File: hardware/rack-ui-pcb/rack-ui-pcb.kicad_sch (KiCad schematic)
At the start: 8 parts, among them J1 IO, J2 Conn_ARM_SWD_TagConnect_TC203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, SW1 RotaryEncoder_Switch_MP, U1 PY32F002AL15S6TU

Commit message: updated schematic & PCB
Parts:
- added H1, H2, H3, H4: MountingHole_M3_3.2mm_Pad, PCM_SL_Mechanical:MountingHole_3.2mm_Pad, symbol PCM_SL_Mechanical:MountingHole_M3_3.2mm_Pad
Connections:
- net +3.3V is gone; now on net +3V3: C3.1, J2.1 (VCC), U1.1 (VCC)
- net SDA is gone; now on net RST: J1.8 (Pin_8), OLED1.4 (SDA)
- net SWD is gone; now on net EncSW: J2.2 (SWDIO), U1.5 (PA13-SWD)
- net EncA: now also U1.2 (PA4/PA10)
- net EncB: now also U1.7 (PA1)
- net GND: now also SW1.MP, H1.1, H2.1, H3.1, H4.1
- net SCL: now also U1.3 (PA3)

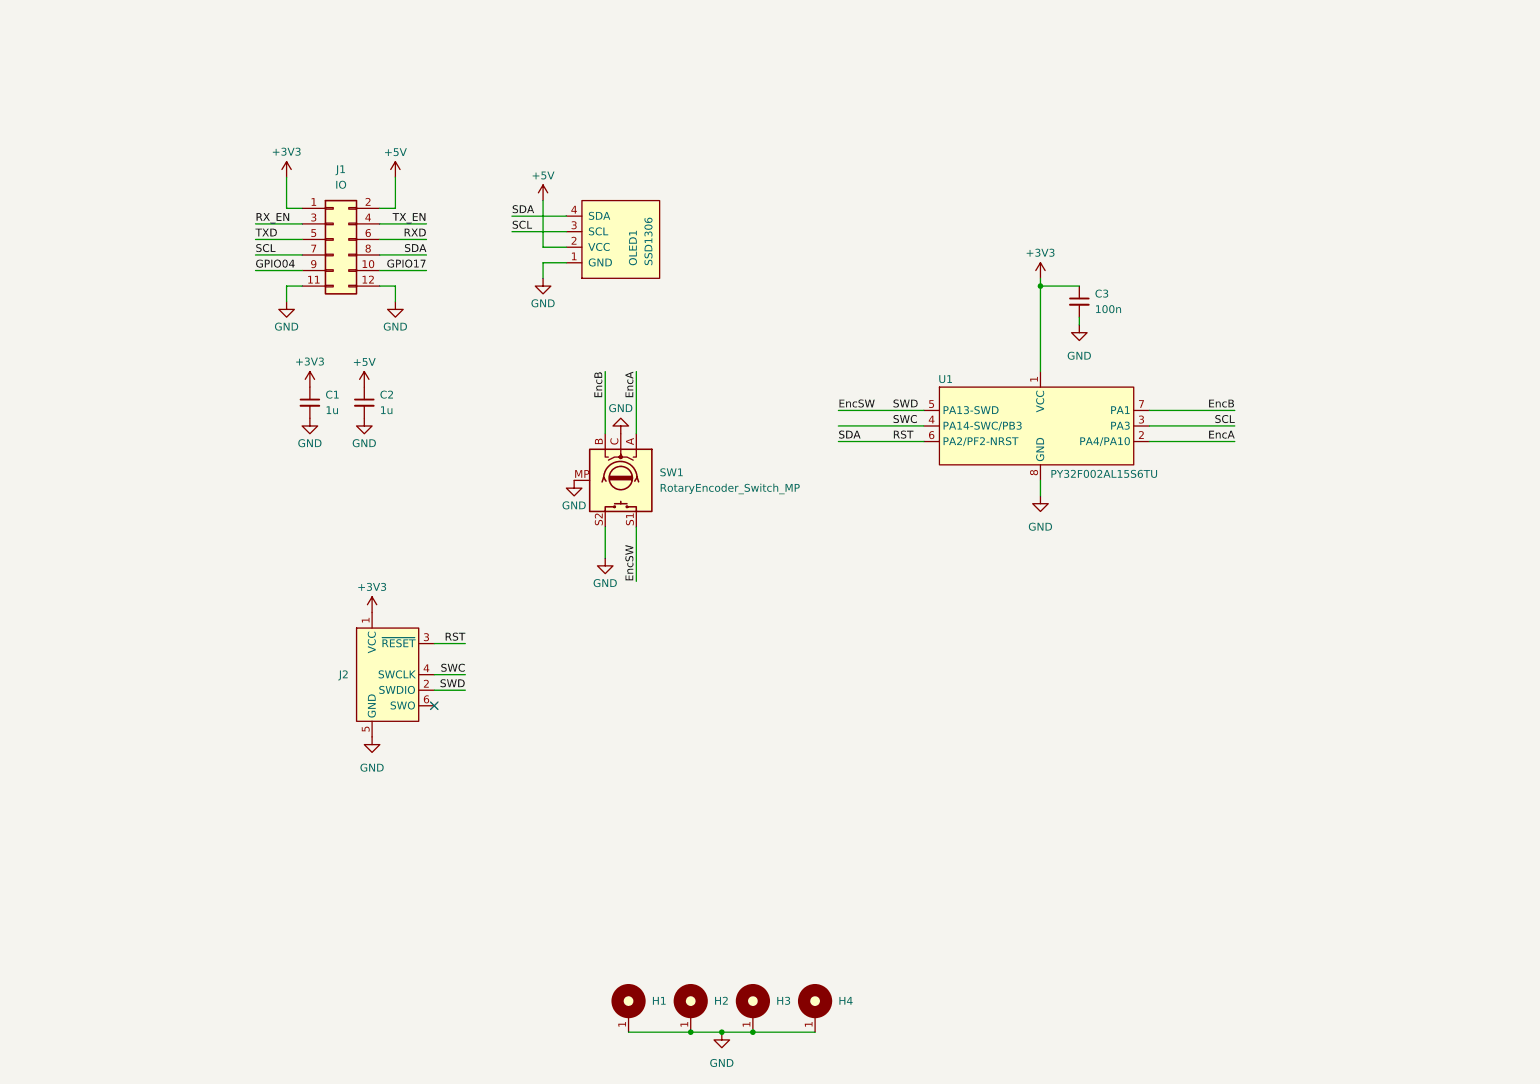
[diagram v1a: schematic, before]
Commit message: updated design wih new uC, added USB-C and UART chip
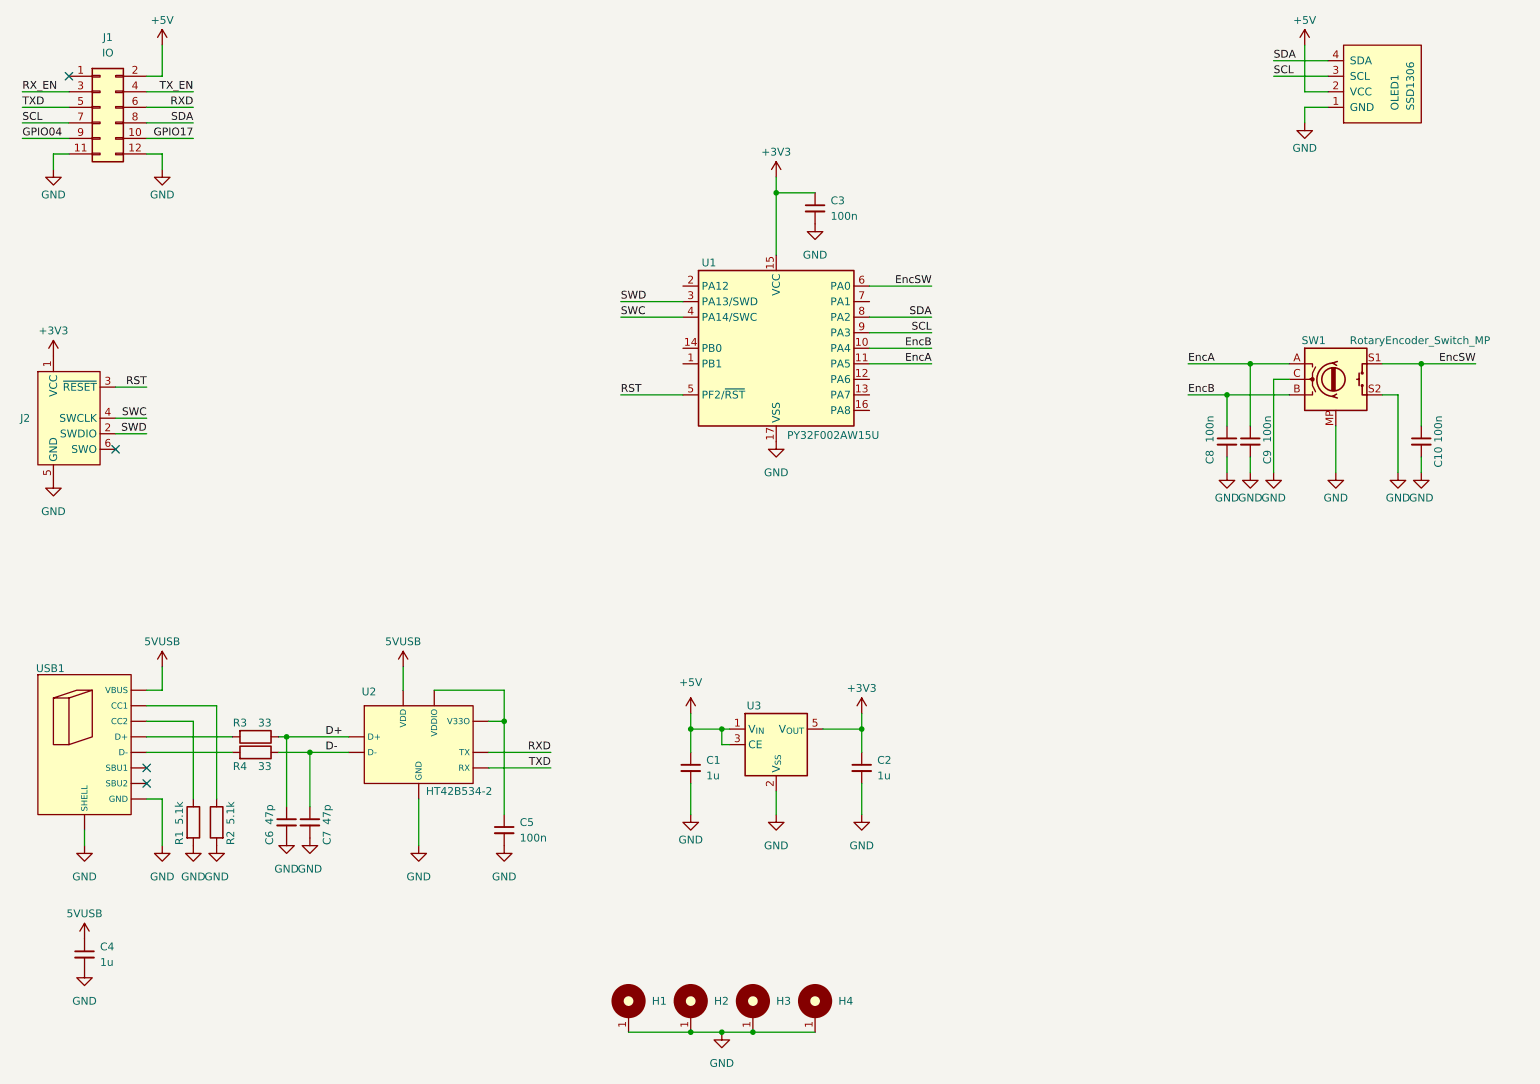
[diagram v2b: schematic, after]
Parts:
- removed U1: PY32F002AL15S6TU, PY32:SOP-8_L4.9-W3.9-P1.27-LS6.0-BL-1, symbol PY32:PY32F002AL15S6TU
- added C10, C5, C8, C9: 100n, Capacitor_SMD:C_0603_1608Metric_Pad1.08x0.95mm_HandSolder, symbol Device:C_Small
- added C4: 1u, Capacitor_SMD:C_0603_1608Metric_Pad1.08x0.95mm_HandSolder, symbol Device:C_Small
- added C6, C7: 47p, Capacitor_SMD:C_0603_1608Metric_Pad1.08x0.95mm_HandSolder, symbol Device:C_Small
- added R1, R2: 5.1k, Resistor_SMD:R_0603_1608Metric_Pad0.98x0.95mm_HandSolder, symbol Device:R
- added R3, R4: 33, Resistor_SMD:R_0603_1608Metric_Pad0.98x0.95mm_HandSolder, symbol Device:R
- added U1: PY32F002AW15U, Package_DFN_QFN:WQFN-16-1EP_3x3mm_P0.5mm_EP1.75x1.75mm, symbol MCU_Puya:PY32F002AW15U
- added U2: HT42B534-2, LCSC:SOP-8_L4.9-W3.9-P1.27-LS6.0-BL, symbol LCSC:HT42B534-2
- added U3: ME6211C33M5G-N, LCSC:SOT-23-5_L3.0-W1.7-P0.95-LS2.8-BL, symbol LCSC:ME6211C33M5G-N
- added USB1: JS16H-TYPE-C449-H105, LCSC:USB-TH_JS16H-TYPE-C449-H105-1, symbol LCSC:JS16H-TYPE-C449-H105
- C1, C2, C3: footprint Capacitor_SMD:C_0402_1005Metric_Pad0.74x0.62mm_HandSolder -> Capacitor_SMD:C_0603_1608Metric_Pad1.08x0.95mm_HandSolder
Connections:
- net +3V3: now also C2.1, U1.15 (VCC), U3.5 (V_{OUT}); no longer C1.1, J1.1 (Pin_1)
- net +5V: now also C1.1, U3.1 (V_{IN}), U3.3 (CE); no longer C2.1
- net EncA: now also C9.1, U1.11 (PA5)
- net EncB: now also C8.1, U1.10 (PA4)
- net EncSW: now also C10.1, U1.6 (PA0); no longer J2.2 (SWDIO)
- net GND: now also C10.2, C4.2, C5.2, C6.2, C7.2, C8.2, C9.2, R1.2, R2.2, U1.17 (VSS), U2.1 (GND), U3.2 (V_{SS}), USB1.1 (SHELL), USB1.2 (SHELL), USB1.3 (SHELL), USB1.4 (SHELL), USB1.A1 (GND), USB1.A12 (GND), USB1.B1 (GND), USB1.B12 (GND)
- net RST: now also U1.5 (PF2/~{RST}); no longer J1.8 (Pin_8), OLED1.4 (SDA)
- net RXD: now also U2.2 (TX)
- net SCL: now also U1.9 (PA3)
- net SWC: now also U1.4 (PA14/SWC)
- net TXD: now also U2.4 (RX)
- new net: R2.1, USB1.A5 (CC1)
- new net: R3.2, USB1.A6 (D+), USB1.B6 (D+)
- new net: R4.2, USB1.A7 (D-), USB1.B7 (D-)
- new net: R1.1, USB1.B5 (CC2)
- new net: C5.1, U2.3 (VDDIO), U2.8 (V33O)
- new net 5VUSB: C4.1, U2.7 (VDD), USB1.A4 (VBUS), USB1.A9 (VBUS), USB1.B4 (VBUS), USB1.B9 (VBUS)
- new net D+: C6.1, R3.1, U2.5 (D+)
- new net D-: C7.1, R4.1, U2.6 (D-)
- new net SDA: J1.8 (Pin_8), OLED1.4 (SDA), U1.8 (PA2)
- new net SWD: J2.2 (SWDIO), U1.3 (PA13/SWD)
- no-connect marks 1 -> 4
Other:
- moved on the sheet: C3, J1, J2, OLED1

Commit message: added charlieplexed LED matrix
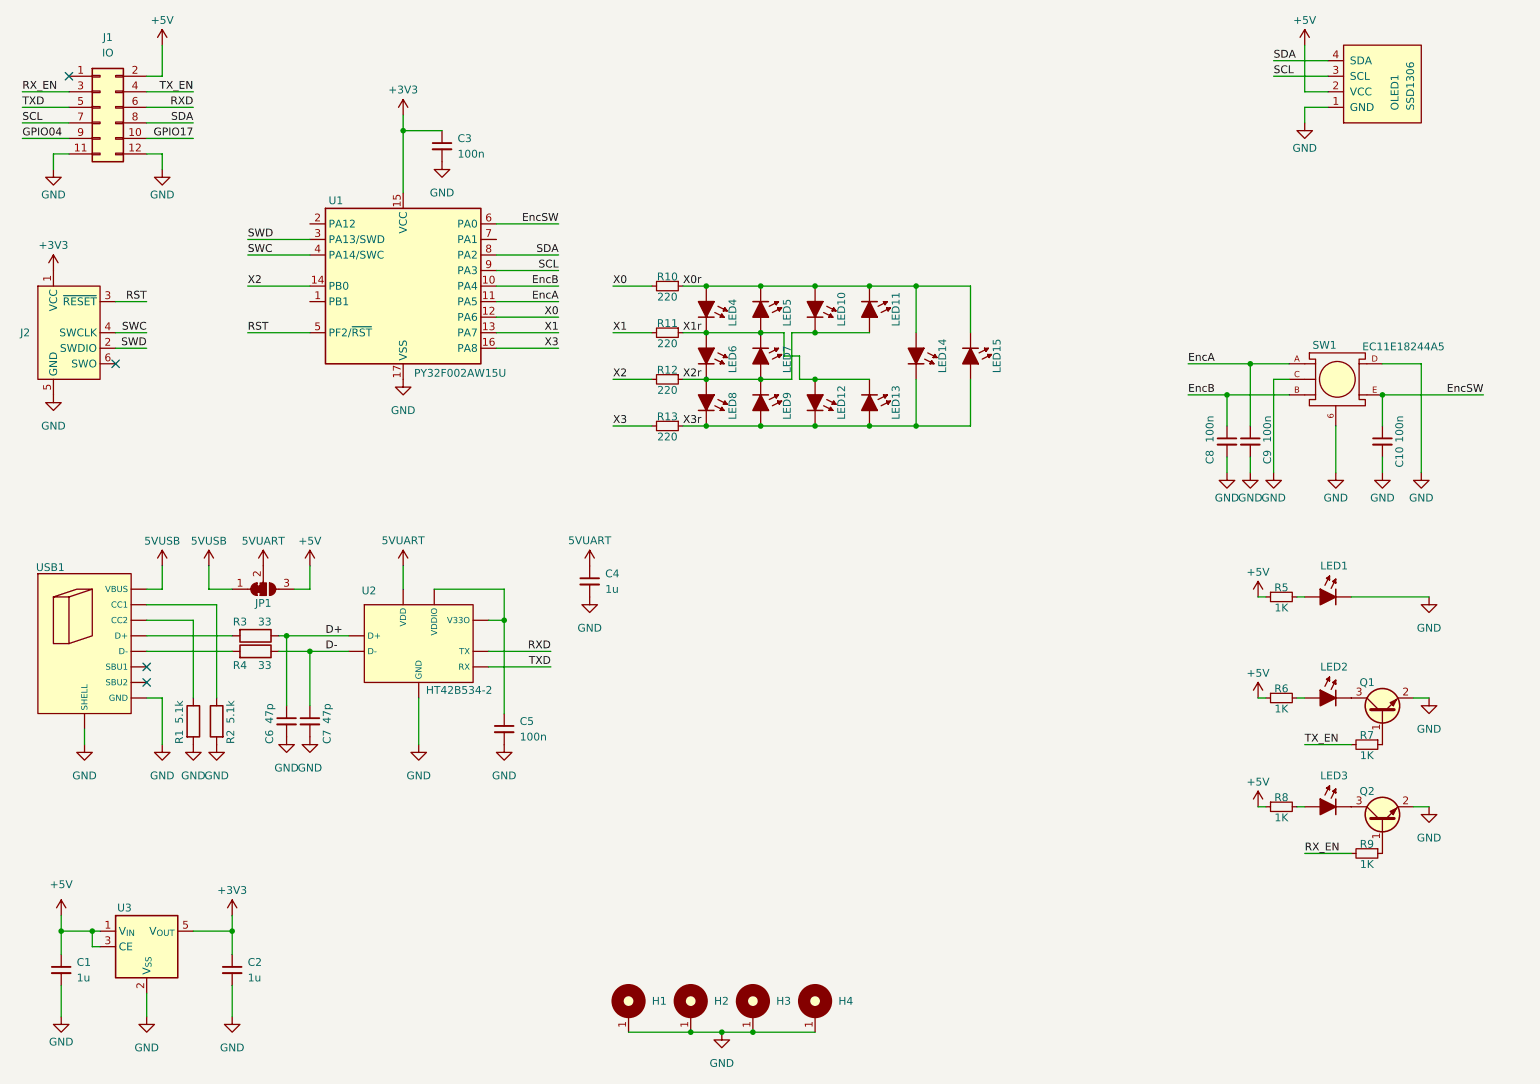
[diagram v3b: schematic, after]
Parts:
- removed SW1: RotaryEncoder_Switch_MP, Rotary_Encoder:RotaryEncoder_Alps_EC11E-Switch_Vertical_H20mm, symbol Device:RotaryEncoder_Switch_MP
- added JP1: SolderJumper_3_Bridged12, Jumper:SolderJumper-3_P1.3mm_Bridged12_RoundedPad1.0x1.5mm, symbol Jumper:SolderJumper_3_Bridged12
- added LED1, LED10, LED11, LED12, LED13, LED14, LED15, LED4, LED5, LED6, LED7, LED8, LED9: Red, PCM_LED_SMD_AKL:LED_0402_1005Metric_Pad0.77x0.64mm, symbol PCM_LED_AKL:LED_0603
- added LED2: Amber, PCM_LED_SMD_AKL:LED_0402_1005Metric_Pad0.77x0.64mm, symbol PCM_LED_AKL:LED_0603
- added LED3: Green, PCM_LED_SMD_AKL:LED_0402_1005Metric_Pad0.77x0.64mm, symbol PCM_LED_AKL:LED_0603
- added Q1, Q2: BC817-40W, Package_TO_SOT_SMD:SOT-323_SC-70, symbol PCM_Transistor_BJT_AKL:BC817-40W
- added R10, R11, R12, R13: 220, Resistor_SMD:R_0603_1608Metric_Pad0.98x0.95mm_HandSolder, symbol Device:R_Small
- added R5, R6, R7, R8, R9: 1K, Resistor_SMD:R_0603_1608Metric_Pad0.98x0.95mm_HandSolder, symbol Device:R_Small
- added SW1: EC11E18244A5, LCSC:SW-TH_EC11E18244A5, symbol LCSC:EC11E18244A5
- J1: footprint Connector_IDC:IDC-Header_2x06_P2.54mm_Horizontal -> Connector_IDC:IDC-Header_2x06_P2.54mm_Vertical
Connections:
- net +5V: now also JP1.3 (B), R5.1, R6.1, R8.1
- net 5VUSB: now also JP1.1 (A); no longer C4.1, U2.7 (VDD)
- net EncA: now also SW1.A
- net EncB: now also SW1.B
- net EncSW: now also SW1.E
- net GND: now also LED1.1 (K), Q1.2 (E), Q2.2 (E), SW1.6, SW1.7, SW1.C, SW1.D
- net RX_EN: now also R9.2
- net TX_EN: now also R7.2
- net X0: now reaches U1.12 (PA6)
- net X0: now also R10.2
- net X1: now reaches U1.13 (PA7)
- net X1: now also R11.2
- net X2: now reaches U1.14 (PB0)
- net X2: now also R12.2
- net X3: now reaches U1.16 (PA8)
- net X3: now also R13.2
- new net: Q1.1 (B), R7.1
- new net: Q2.1 (B), R9.1
- new net: LED3.1 (K), Q2.3 (C)
- new net: LED2.1 (K), Q1.3 (C)
- new net: LED2.2 (A), R6.2
- new net: LED1.2 (A), R5.2
- new net: LED3.2 (A), R8.2
- new net 5VUART: C4.1, JP1.2 (C), U2.7 (VDD)
- new net X0r: LED10.2 (A), LED11.1 (K), LED14.2 (A), LED15.1 (K), LED4.2 (A), LED5.1 (K), R10.1
- new net X1r: LED12.2 (A), LED13.1 (K), LED4.1 (K), LED5.2 (A), LED6.2 (A), LED7.1 (K), R11.1
- new net X2r: LED10.1 (K), LED11.2 (A), LED6.1 (K), LED7.2 (A), LED8.2 (A), LED9.1 (K), R12.1
- new net X3r: LED12.1 (K), LED13.2 (A), LED14.1 (K), LED15.2 (A), LED8.1 (K), LED9.2 (A), R13.1
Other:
- moved on the sheet: C1, C10, C2, C3, C4, C5, C6, C7, J2, R1, R2, R3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

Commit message: updated white LED footprints
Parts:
- LED10, LED11, LED12, LED13, LED14, LED15, LED5, LED6, LED7, LED8, LED9: footprint PCM_LED_SMD_AKL:LED_0402_1005Metric_Pad0.77x0.64mm -> LED_SMD:LED_0805_2012Metric_Pad1.15x1.40mm_HandSolder
- LED4: value Red -> SZYY0805W; footprint PCM_LED_SMD_AKL:LED_0402_1005Metric_Pad0.77x0.64mm -> LED_SMD:LED_0805_2012Metric_Pad1.15x1.40mm_HandSolder; LCSC Part C7496803 -> C434434
- R10, R11, R12, R13: value 220 -> 120
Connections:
- net X2: now also U1.2 (PA12); no longer U1.14 (PB0)
- no-connect marks 4 -> 7
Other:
- moved on the sheet: C3, C4, LED10, LED11, LED12, LED13, LED14, LED15, LED4, LED5, LED6, LED7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

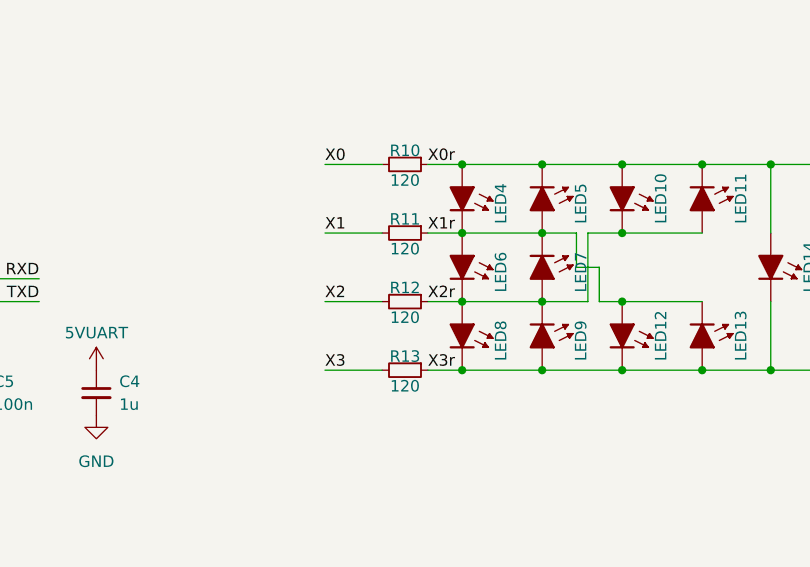
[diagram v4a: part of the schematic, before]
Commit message: updated footprints, part numbers
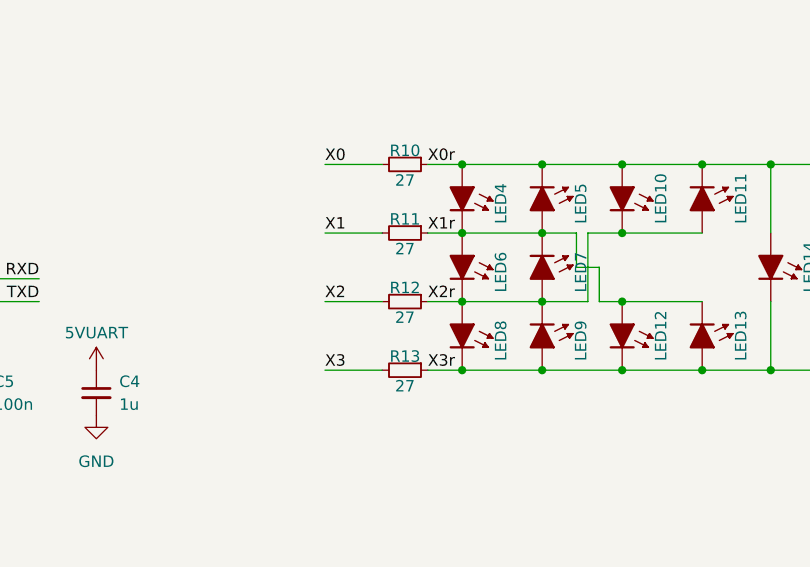
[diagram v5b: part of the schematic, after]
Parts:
- C1, C2, C4: LCSC (none) -> C59302; LCSC Part C29266 -> C59302
- C10, C3, C5, C8, C9: LCSC (none) -> C235731; LCSC Part C60474 -> C235731
- C6, C7: LCSC (none) -> C1671; LCSC Part C60474 -> C1671
- J1: LCSC (none) -> C109410; LCSC Part (none) -> C109410; now in the parts list
- LED1: footprint PCM_LED_SMD_AKL:LED_0402_1005Metric_Pad0.77x0.64mm -> PCM_SparkFun-LED:LED_0603_1608Metric_Red; LCSC (none) -> C52675987; LCSC Part C7496803 -> C52675987
- LED10, LED11, LED12, LED13, LED14, LED15, LED5, LED6, LED7, LED8, LED9: value Red -> SZYY0805W; LCSC (none) -> C434434; LCSC Part C7496803 -> C434434
- LED2: footprint PCM_LED_SMD_AKL:LED_0402_1005Metric_Pad0.77x0.64mm -> PCM_SparkFun-LED:LED_0603_1608Metric_Orange; LCSC (none) -> C165983; LCSC Part C5123495 -> C165983
- LED3: footprint PCM_LED_SMD_AKL:LED_0402_1005Metric_Pad0.77x0.64mm -> PCM_SparkFun-LED:LED_0603_1608Metric_Green; LCSC (none) -> C51933293; LCSC Part C74338 -> C51933293
- LED4: LCSC (none) -> C434434
- OLED1: now left out of the parts list
- Q1, Q2: LCSC (none) -> C383187
- R1, R2: LCSC (none) -> C2907114; LCSC Part (none) -> C2907114
- R10, R11, R12, R13: value 120 -> 27; LCSC (none) -> C2907136; LCSC Part C106235 -> C2907136
- R3, R4: LCSC (none) -> C2907154; LCSC Part (none) -> C2907154
- R5, R6, R7, R8, R9: LCSC (none) -> C2907002; LCSC Part C106235 -> C2907002
- SW1: LCSC Part (none) -> C255515
- U1: LCSC (none) -> C5291740; LCSC Part (none) -> C5291740
- U2: LCSC Part (none) -> C493294
- U3: LCSC Part (none) -> C82942
- USB1: LCSC Part (none) -> C49118459
